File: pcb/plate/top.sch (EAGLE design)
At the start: 27 parts

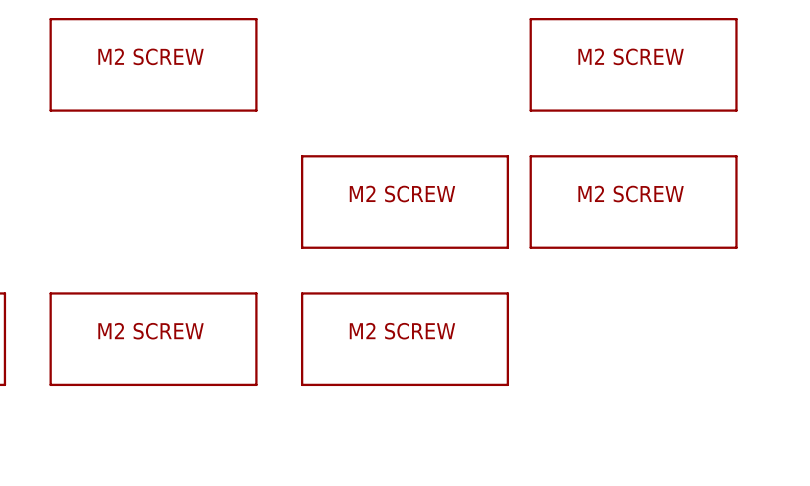
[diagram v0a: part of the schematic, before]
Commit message: adjusted top plate cutout, removed unused screw hole
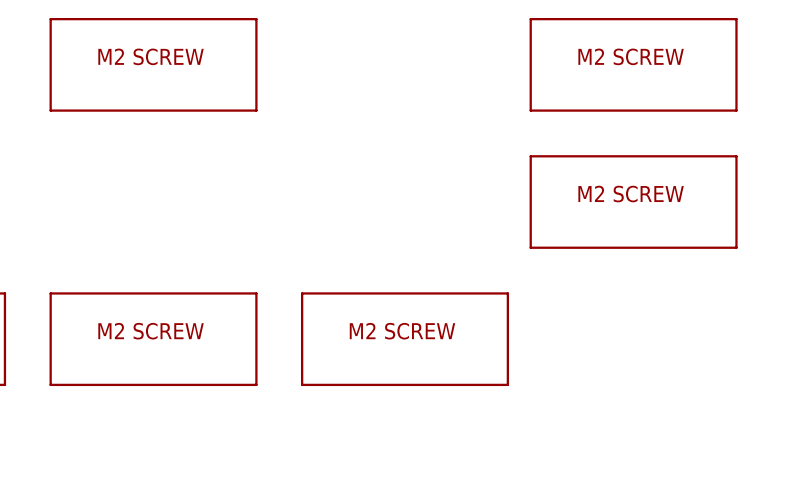
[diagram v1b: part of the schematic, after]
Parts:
- removed U$17: M2_SCREW_DEV, duckypad:M2_SCREW_DEV
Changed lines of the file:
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@@
 <part name="U$12" library="duckypad" deviceset="M2_SCREW_DEV" device=""/>
 <part name="U$13" library="duckypad" deviceset="M2_SCREW_DEV" device=""/>
-<part name="U$17" library="duckypad" deviceset="M2_SCREW_DEV" device=""/>
 <part name="U$14" library="duckypad" deviceset="M2_SCREW_DEV" device=""/>
 <part name="U$22" library="duckypad" deviceset="M2_SCREW_DEV" device=""/>
@@
 <instance part="U$12" gate="G$1" x="127" y="292.1" smashed="yes"/>
 <instance part="U$13" gate="G$1" x="154.94" y="292.1" smashed="yes"/>
-<instance part="U$17" gate="G$1" x="182.88" y="307.34" smashed="yes"/>
 <instance part="U$14" gate="G$1" x="208.28" y="322.58" smashed="yes"/>
 <instance part="U$22" gate="G$1" x="208.28" y="307.34" smashed="yes"/>
